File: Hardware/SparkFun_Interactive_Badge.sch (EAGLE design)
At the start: 19 parts, among them Q1 DMG2307L, U1 MIC5205-3.3V

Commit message: Finished initial sch. Mock-up layout
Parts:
- added C4, C5, C6, C7, C8: 0.1uF, SparkFun-Capacitors:0.1UF-25V(+80/-20%)(0603)
- added D3: GREEN, SparkFun-LED:LED-GREEN0603
- added JP3: M12LOCK, SparkFun-Connectors:M12LOCK
- added JP4: M14LOCK, SparkFun-Connectors:M14LOCK
- added JP5: M02PTH, SparkFun-Connectors:M02PTH
- added JP6: 1x3 RA Female .1", SparkFun-Connectors:M03SMD_RA_FEMALE
- added R3: 10K, SparkFun-Resistors:10KOHM-1/10W-1%(0603)0603
- added R4: 330, SparkFun-Resistors:330OHM1/10W1%(0603)
- added S1: SWITCH-MOMENTARY-2SMD, SparkFun-Electromechanical:SWITCH-MOMENTARY-2SMD
- added U2: ATMEGA328P, SparkFun-DigitalIC:ATMEGA328_SMT
- added U3: CY7C65213, SparkFun-DigitalIC:CY7C65213
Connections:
- new net A0: U2.PC0(ADC0)
- new net A1: U2.PC1(ADC1)
- new net A2: U2.PC2(ADC2)
- new net A3: U2.PC3(ADC3)
- new net A4: U2.PC4(ADC4/SDA)
- new net A5: U2.PC5(ADC5/SCL)
- new net A6: U2.ADC6
- new net A7: U2.ADC7
- new net AREF: C5.1, U2.AREF
- new net D+: JP1.D+, U3.USBDP
- new net D-: JP1.D-, U3.USBDM
- new net D10: U2.PB2(SS/OC1B)
- new net D2: U2.PD2(INT0)
- new net D3: U2.PD3(INT1)
- new net D4: U2.PD4(XCK/T0)
- new net D5: U2.PD5(T1)
- new net D6: U2.PD6(AIN0)
- new net D7: U2.PD7(AIN1)
- new net D8: U2.PB0(ICP)
- new net D9: U2.PB1(OC1A)
- new net DTR: C4.1, U3.DTR
- new net MISO: U2.PB4(MISO)
- new net MOSI: U2.PB3(MOSI/OC2)
- new net N$1: D3.A, R4.1
- new net N$10: JP3.6
- new net N$11: JP3.5
- new net N$12: JP3.4
- new net N$13: JP3.3
- new net N$14: JP3.2
- new net N$15: JP3.1
- new net N$16: JP4.1
- new net N$17: JP4.2
- new net N$18: JP4.3
- new net N$19: JP4.4
- new net N$2: C8.1, U3.VCCD
- new net N$20: JP4.5
- new net N$21: JP4.6
- new net N$22: JP4.7
- new net N$23: JP4.8
- new net N$24: JP4.9
- new net N$25: JP4.10
- new net N$26: JP4.11
- new net N$27: JP4.12
- new net N$28: JP4.13
- new net N$29: JP4.14
- new net N$3: JP3.12
- new net N$30: JP5.2
- new net N$31: JP5.1
- new net N$5: JP3.11
- new net N$6: JP3.10
- new net N$7: JP3.9
- new net N$8: JP3.8
- new net N$9: JP3.7
- new net RESET: C4.2, R3.1, S1.2, U2.PC6(/RESET)
- new net RXI: U2.PD0(RXD), U3.TXD
- new net SCK: R4.2, U2.PB5(SCK)
- new net TXO: U2.PD1(TXD), U3.RXD
- net 3.3V: now also U3.VCCIO
- net 5V: now also C7.1, U3.VCC
- net GND: now also C5.2, C6.2, C7.2, C8.2, D3.C, S1.1, U2.AGND, U2.GND@1, U2.GND@2, U3.AGND, U3.CTS, U3.GND18, U3.GND21, U3.GND7, U3.TEST
- net VCC: now also C6.1, R3.2, U2.AVCC, U2.VCC@1, U2.VCC@2
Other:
- moved on the sheet: D1, JP2, Q1, R1

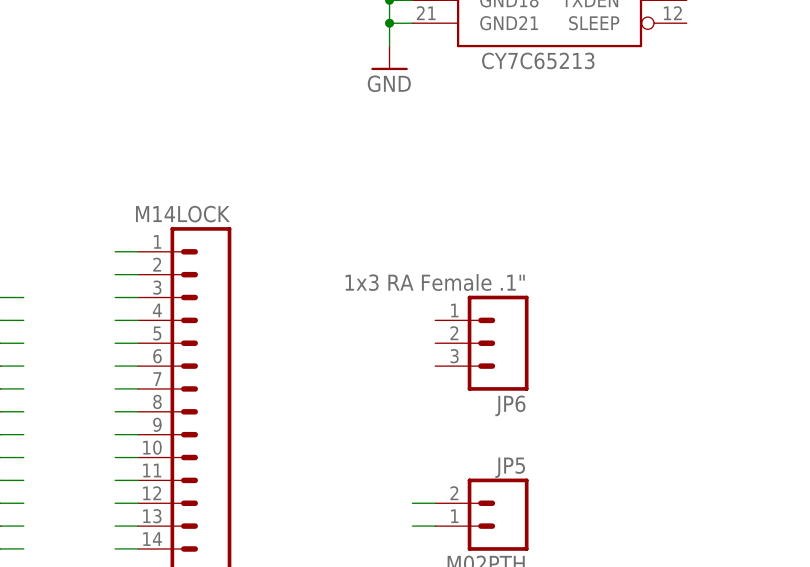
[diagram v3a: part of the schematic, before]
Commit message: Added PTH UART header on bottom. Added outline of wing on tDocu layer.
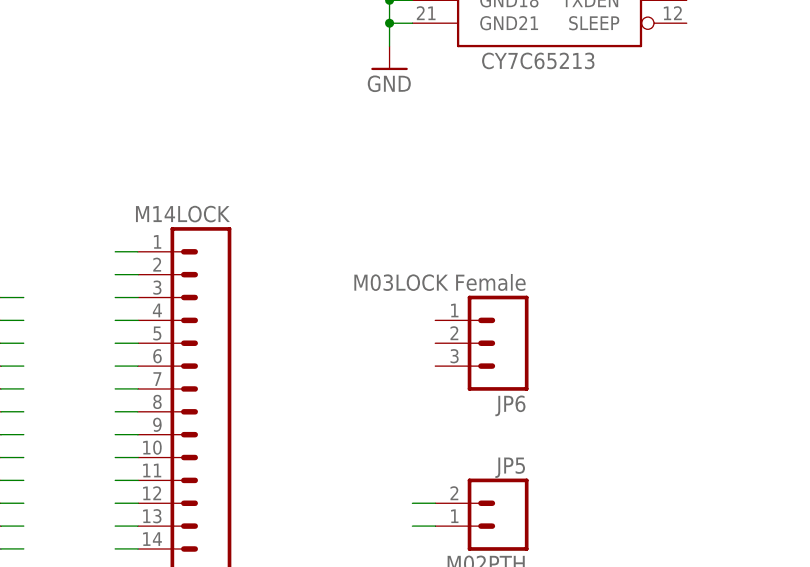
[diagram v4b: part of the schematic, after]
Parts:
- JP6: value 1x3 RA Female .1" -> M03LOCK Female; device SparkFun-Connectors:M03SMD_RA_FEMALE -> SparkFun-Connectors:M03LOCK
- S1: value SWITCH-MOMENTARY-2SMD -> SWITCH-MOMENTARY-2SMD-REDUNDANT; device SparkFun-Electromechanical:SWITCH-MOMENTARY-2SMD -> SparkFun-Electromechanical:SWITCH-MOMENTARY-2SMD-REDUNDANT
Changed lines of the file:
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@@
 <setting verticaltext="up"/>
 </settings>
-<grid distance="0.1" unitdist="inch" unit="inch" style="lines" multiple="1" display="yes" altdistance="0.01" altunitdist="inch" altunit="inch"/>
+<grid distance="0.1" unitdist="inch" unit="inch" style="lines" multiple="1" display="no" altdistance="0.01" altunitdist="inch" altunit="inch"/>
 <layers>
 <layer number="1" name="Top" color="4" fill="1" visible="no" active="no"/>
@@
 <part name="U2" library="SparkFun-DigitalIC" deviceset="ATMEGA328_SMT" device="" value="ATMEGA328P"/>
 <part name="C4" library="SparkFun-Capacitors" deviceset="0.1UF-25V(+80/-20%)(0603)" device="" value="0.1uF"/>
-<part name="S1" library="SparkFun-Electromechanical" deviceset="SWITCH-MOMENTARY-2" device="SMD">
+<part name="S1" library="SparkFun-Electromechanical" deviceset="SWITCH-MOMENTARY-2" device="SMD-REDUNDANT" value="SWITCH-MOMENTARY-2SMD-REDUNDANT">
 <attribute name="FUNC" value="Reset"/>
 </part>
@@
 <part name="JP4" library="SparkFun-Connectors" deviceset="M14" device="LOCK"/>
 <part name="JP5" library="SparkFun-Connectors" deviceset="M02" device="PTH"/>
-<part name="JP6" library="SparkFun-Connectors" deviceset="M03" device="SMD_RA_FEMALE" value="1x3 RA Female .1&quot;"/>
+<part name="JP6" library="SparkFun-Connectors" deviceset="M03" device="LOCK" value="M03LOCK Female"/>
 </parts>
 <sheets>

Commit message: Initial layout complete
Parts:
- JP2, JP5: value M02PTH -> M021X02_NO_SILK; device SparkFun-Connectors:M02PTH -> SparkFun-Connectors:M021X02_NO_SILK
- JP3: value M12LOCK -> M13LOCK_NO_SILK; device SparkFun-Connectors:M12LOCK -> SparkFun-Connectors:M13LOCK_NO_SILK
- JP4: value M14LOCK -> M15LOCK_NO_SILK; device SparkFun-Connectors:M14LOCK -> SparkFun-Connectors:M15LOCK_NO_SILK
- JP6: device SparkFun-Connectors:M03LOCK -> SparkFun-Connectors:M03LOCK_NO_SILK
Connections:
- removed net N$10: JP3.6
- removed net N$11: JP3.5
- removed net N$12: JP3.4
- removed net N$13: JP3.3
- removed net N$14: JP3.2
- removed net N$15: JP3.1
- removed net N$16: JP4.1
- removed net N$17: JP4.2
- removed net N$18: JP4.3
- removed net N$19: JP4.4
- removed net N$20: JP4.5
- removed net N$21: JP4.6
- removed net N$22: JP4.7
- removed net N$23: JP4.8
- removed net N$24: JP4.9
- removed net N$25: JP4.10
- removed net N$26: JP4.11
- removed net N$27: JP4.12
- removed net N$28: JP4.13
- removed net N$29: JP4.14
- removed net N$3: JP3.12
- removed net N$30: JP5.2
- removed net N$31: JP5.1
- removed net N$5: JP3.11
- removed net N$6: JP3.10
- removed net N$7: JP3.9
- removed net N$8: JP3.8
- removed net N$9: JP3.7
- net 3.3V: now also JP4.2
- net 5V: now also JP4.1
- net A0: now also JP4.11
- net A1: now also JP4.10
- net A2: now also JP4.9
- net A3: now also JP4.8
- net A4: now also JP4.7
- net A5: now also JP4.6
- net A6: now also JP5.1
- net A7: now also JP5.2
- net D10: now also JP4.15, JP6.1
- net D2: now also JP3.8
- net D3: now also JP3.7
- net D4: now also JP3.6
- net D5: now also JP3.5
- net D6: now also JP3.4
- net D7: now also JP3.3
- net D8: now also JP3.2
- net D9: now also JP3.1
- net DTR: now also JP3.13
- net GND: now also JP3.9, JP4.3, JP6.2
- net MISO: now also JP4.13
- net MOSI: now also JP4.14, JP6.3
- net RESET: now also JP3.10, JP4.4
- net RXI: now also JP3.11
- net SCK: now also JP4.12
- net TXO: now also JP3.12
- net VCC: now also JP4.5
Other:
- note added: "A6/A7 Headers"
- note added: "GPIO Headers"
- note added: "Microcontroller"
- note added: "RX (Pin 10)"
- note added: "Software Serial"
- note added: "TX (Pin 11)"
- note added: "USB Plug"
- note added: "USB-UART"
- note added: "Voltage Regulator"
- note added: "Voltage Selector"
- moved on the sheet: C1, C2, C3, C5, C6, D1, D2, D3, JP1, JP2, JP5, JP6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

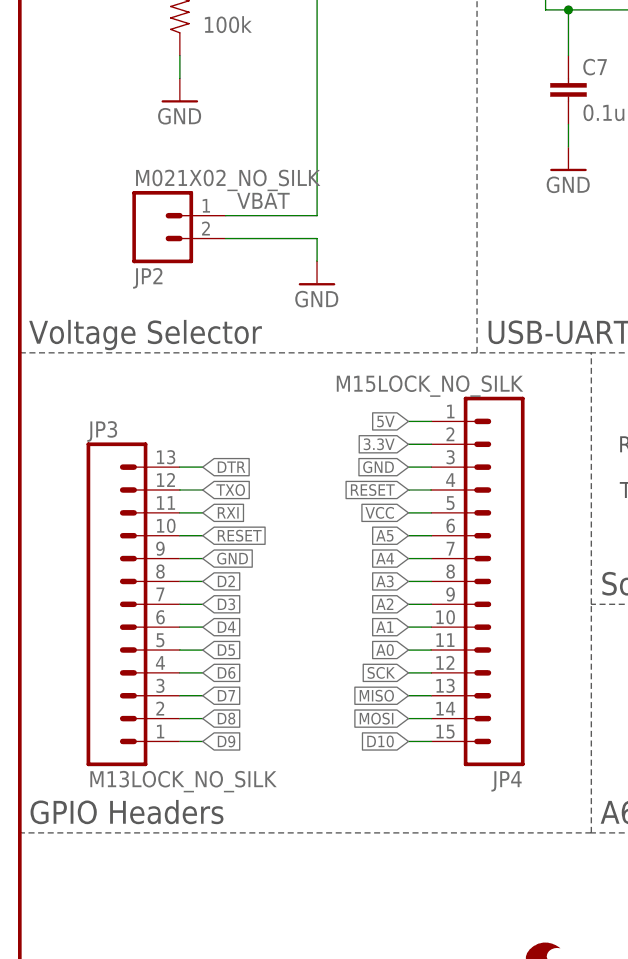
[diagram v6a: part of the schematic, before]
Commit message: Moved pins. Added silk.
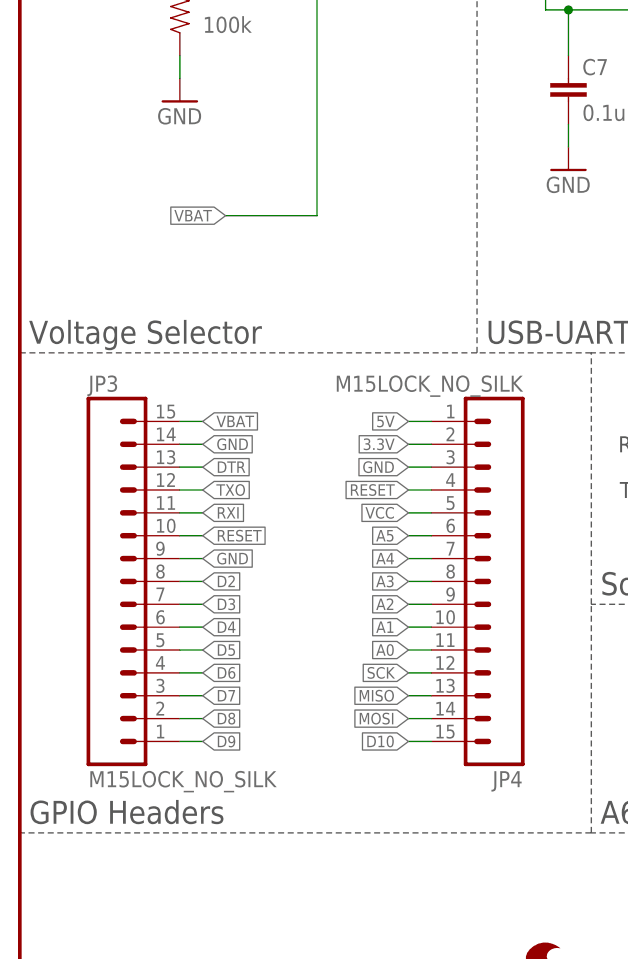
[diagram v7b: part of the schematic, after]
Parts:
- removed JP2: M021X02_NO_SILK, SparkFun-Connectors:M021X02_NO_SILK
- JP3: value M13LOCK_NO_SILK -> M15LOCK_NO_SILK; device SparkFun-Connectors:M13LOCK_NO_SILK -> SparkFun-Connectors:M15LOCK_NO_SILK
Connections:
- net GND: now also JP3.14; no longer JP2.2
- net VBAT: now also JP3.15; no longer JP2.1
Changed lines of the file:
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@@
 <setting verticaltext="up"/>
 </settings>
-<grid distance="0.1" unitdist="inch" unit="inch" style="lines" multiple="1" display="no" altdistance="0.01" altunitdist="inch" altunit="inch"/>
+<grid distance="0.1" unitdist="inch" unit="inch" style="lines" multiple="1" display="yes" altdistance="0.01" altunitdist="inch" altunit="inch"/>
 <layers>
 <layer number="1" name="Top" color="4" fill="1" visible="no" active="no"/>
@@
 <part name="GND15" library="SparkFun-Aesthetics" deviceset="GND" device=""/>
 <part name="SUPPLY1" library="SparkFun-Aesthetics" deviceset="VCC" device=""/>
-<part name="JP2" library="SparkFun-Connectors" deviceset="M02" device="1X02_NO_SILK" value="M021X02_NO_SILK"/>
-<part name="GND1" library="SparkFun-Aesthetics" deviceset="GND" device=""/>
 <part name="SUPPLY2" library="SparkFun-Aesthetics" deviceset="3.3V" device=""/>
 <part name="U1" library="SparkFun-PowerIC" deviceset="MIC5205" device="3.3V" value="MIC5205-3.3V"/>
@@
 <part name="JP6" library="SparkFun-Connectors" deviceset="M03" device="LOCK_NO_SILK" value="M03LOCK Female"/>
 <part name="JP4" library="SparkFun-Connectors" deviceset="M15" device="LOCK_NO_SILK" value="M15LOCK_NO_SILK"/>
-<part name="JP3" library="SparkFun-Connectors" deviceset="M13" device="LOCK_NO_SILK" value="M13LOCK_NO_SILK"/>
+<part name="JP3" library="SparkFun-Connectors" deviceset="M15" device="LOCK_NO_SILK"/>
 </parts>
 <sheets>
@@
 <instance part="GND15" gate="1" x="17.78" y="109.22"/>
 <instance part="SUPPLY1" gate="G$1" x="33.02" y="142.24"/>
-<instance part="JP2" gate="G$1" x="15.24" y="96.52" rot="MR180"/>
-<instance part="GND1" gate="1" x="33.02" y="88.9"/>
 <instance part="SUPPLY2" gate="G$1" x="17.78" y="142.24"/>
 <instance part="U1" gate="G$1" x="88.9" y="167.64"/>
@@
 <instance part="JP6" gate="G$1" x="96.52" y="68.58" rot="R180"/>
 <instance part="JP4" gate="G$1" x="55.88" y="55.88" rot="R180"/>
-<instance part="JP3" gate="G$1" x="7.62" y="53.34"/>
+<instance part="JP3" gate="G$1" x="7.62" y="55.88"/>
 </instances>
 <busses>
@@
 <pinref part="GND15" gate="1" pin="GND"/>
 <wire x1="17.78" y1="114.3" x2="17.78" y2="111.76" width="0.1524" layer="91"/>
-</segment>
-<segment>
-<pinref part="JP2" gate="G$1" pin="2"/>
-<wire x1="22.86" y1="93.98" x2="33.02" y2="93.98" width="0.1524" layer="91"/>
-<pinref part="GND1" gate="1" pin="GND"/>
-<wire x1="33.02" y1="93.98" x2="33.02" y2="91.44" width="0.1524" layer="91"/>
 </segment>
 <segment>
@@
 <label x="86.36" y="68.58" size="1.27" layer="95" rot="R180" xref="yes"/>
 </segment>
+<segment>
+<pinref part="JP3" gate="G$1" pin="14"/>
+<wire x1="17.78" y1="71.12" x2="20.32" y2="71.12" width="0.1524" layer="91"/>
+<label x="20.32" y="71.12" size="1.27" layer="95" xref="yes"/>
+</segment>
 </net>
 <net name="VBAT" class="0">
@@
 <wire x1="22.86" y1="96.52" x2="33.02" y2="96.52" width="0.1524" layer="91"/>
 <wire x1="33.02" y1="96.52" x2="33.02" y2="121.92" width="0.1524" layer="91"/>
-<pinref part="JP2" gate="G$1" pin="1"/>
-<label x="24.13" y="97.282" size="1.778" layer="95"/>
+<label x="22.86" y="96.52" size="1.27" layer="95" rot="R180" xref="yes"/>
+</segment>
+<segment>
+<pinref part="JP3" gate="G$1" pin="15"/>
+<wire x1="17.78" y1="73.66" x2="20.32" y2="73.66" width="0.1524" layer="91"/>
+<label x="20.32" y="73.66" size="1.27" layer="95" xref="yes"/>
 </segment>
 </net>
@@
 </segment>
 <segment>
-<pinref part="JP3" gate="G$1" pin="13"/>
 <wire x1="17.78" y1="68.58" x2="20.32" y2="68.58" width="0.1524" layer="91"/>
 <label x="20.32" y="68.58" size="1.27" layer="95" xref="yes"/>
-</segment>
-</net>
+<pinref part="JP3" gate="G$1" pin="13"/>
+</segment>
+</net>
